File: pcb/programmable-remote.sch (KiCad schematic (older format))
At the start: 36 parts

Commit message: Initial schematic done.
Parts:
- removed R?: 20, symbol Device:R
- added Q1: Q_NPN_Darlington_BCE, Package_TO_SOT_SMD:TSOT-23_HandSoldering, symbol Device:Q_NPN_Darlington_BCE
- added R3: 10, Resistor_SMD:R_0603_1608Metric_Pad0.98x0.95mm_HandSolder, symbol Device:R
- added R4: 68k, Resistor_SMD:R_0603_1608Metric_Pad0.98x0.95mm_HandSolder, symbol Device:R
- added R7, R8: 4.7k, Resistor_SMD:R_0603_1608Metric_Pad0.98x0.95mm_HandSolder, symbol Device:R
- added SW8: SW_DIP_x02, programmable-remote:SW_2LP, symbol Switch:SW_DIP_x02
- 500m1: renamed from 500m; footprint (none) -> Fuse:Fuse_0603_1608Metric_Pad1.05x0.95mm_HandSolder
- BT1: renamed from BT?; footprint (none) -> programmable-remote:Battery
- C1, C10, C11, C2, C3, C4, C5, C6, C7, C8, C9: renamed from C?; footprint (none) -> Capacitor_SMD:C_0603_1608Metric_Pad1.08x0.95mm_HandSolder
- D1, D2: renamed from D?; footprint (none) -> Capacitor_SMD:C_0805_2012Metric_Pad1.18x1.45mm_HandSolder
- D3, D4: renamed from D?; footprint (none) -> Diode_SMD:D_1206_3216Metric_Pad1.42x1.75mm_HandSolder
- D5: renamed from D?; footprint (none) -> LED_THT:LED_D3.0mm_IRGrey
- J1: renamed from J?; footprint (none) -> Connector_PinHeader_2.54mm:PinHeader_1x04_P2.54mm_Vertical
- J2: renamed from J?; footprint (none) -> Connector_PinHeader_2.54mm:PinHeader_1x01_P2.54mm_Vertical
- R1, R2, R5, R6: renamed from R?; footprint (none) -> Resistor_SMD:R_0603_1608Metric_Pad0.98x0.95mm_HandSolder
- SW1, SW3, SW4, SW5, SW6, SW7: renamed from SW?; footprint (none) -> Button_Switch_Keyboard:SW_Cherry_MX_1.00u_PCB
- SW2: renamed from SW?; footprint (none) -> programmable-remote:SW_PTS526
- U2: renamed from U?; footprint (none) -> Package_SO:SOIC-8_3.9x4.9mm_P1.27mm
- Y1: renamed from Y?; footprint (none) -> programmable-remote:Crystal_ABLS-8.000MHZ-B4-T
- gave numbers to parts that had none: 2
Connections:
- net GND: now also Q1.3 (E), R7.2, R8.2; no longer D5.1 (K)
- net IR_OUT: now also R4.2
- net V3_3: now also D5.2 (A), SW8.1, SW8.2
- net BOOT1: now reaches U1.28 (PB2)
- net BOOT1: now also R7.1, SW8.3
- net BOOT0: now reaches U1.60 (BOOT0)
- net BOOT0: now also R8.1, SW8.4
- new net: D5.1 (K), R3.2
- new net: Q1.1 (B), R4.1
- new net: Q1.2 (C), R3.1
- no-connect marks 0 -> 33
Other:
- note added: "Assume saturation for the following:\nI_ledmax = 100 mA\nR_collector = (V3_3 - V_led - V_transistor)/l_ledmax\nR_collector = (3.3 - 1.42 - 1)/0.1 ohm = 8.8 ohm\nI_base = I_ledmax/Hfe*ODF = .1/50000*10 A = 20 uA\nR_base = (V3_3 - V_be) / I_base\n= (3.3 - 2) / 0.00002 ohm = 65 kohm\n"
- note added: "Switches"
- note removed: "Buttons"
- moved on the sheet: C8, D1, D2, D5, J2, R1, R2, R5, SW1, SW2, SW3, SW4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

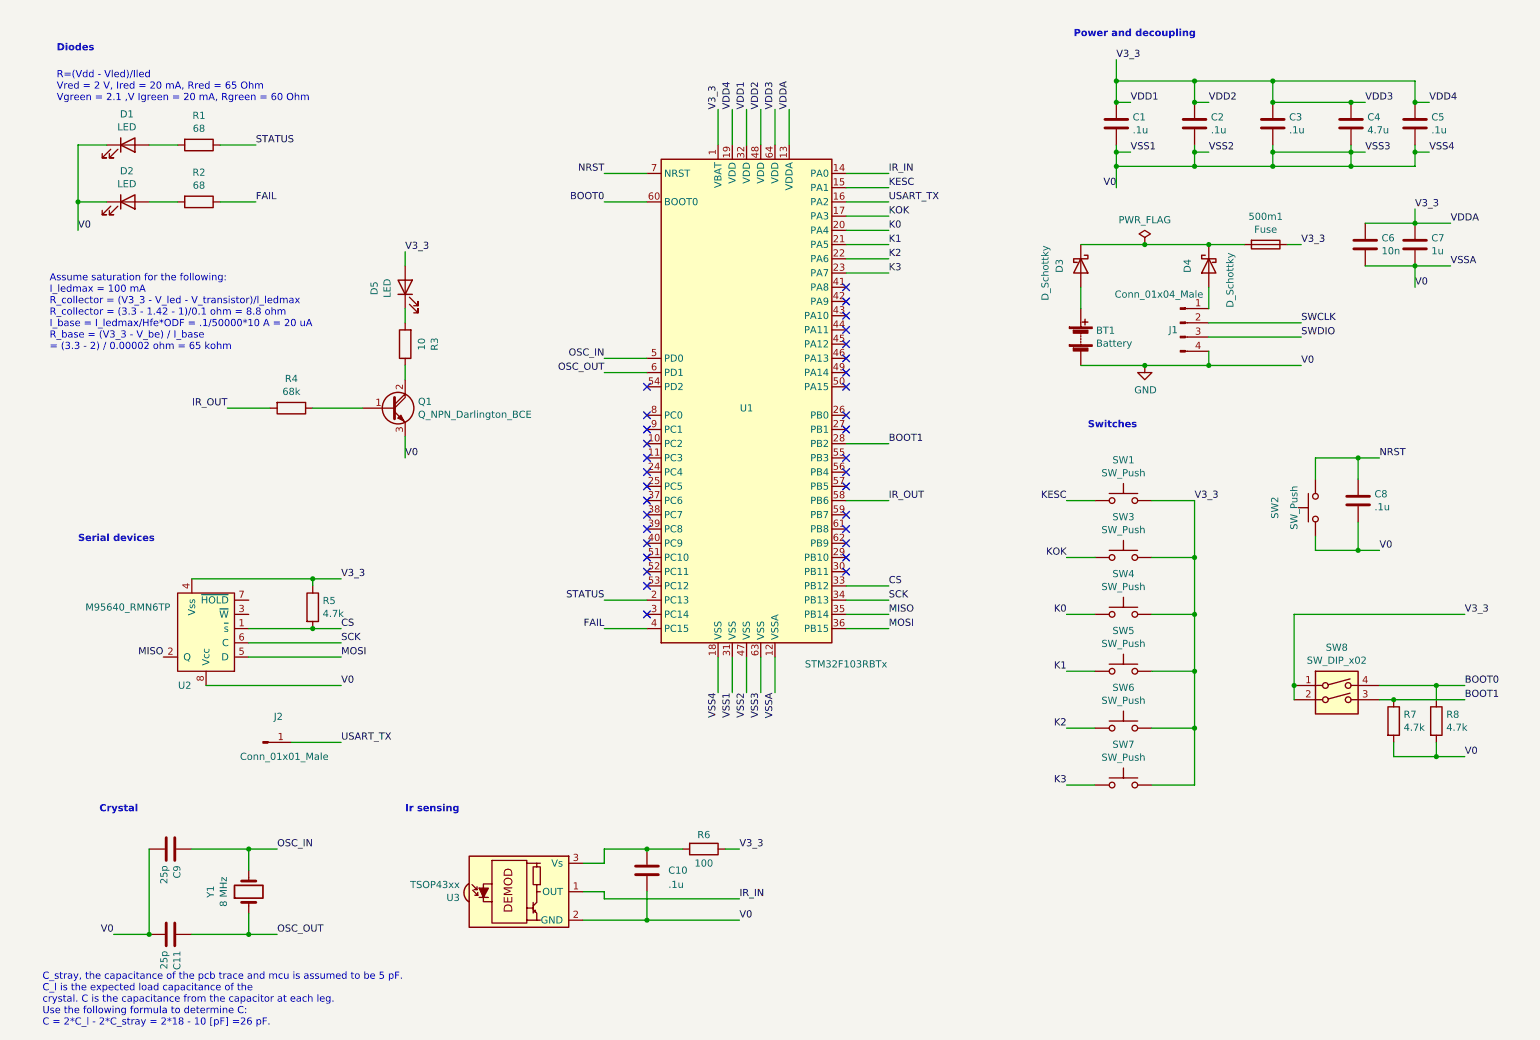
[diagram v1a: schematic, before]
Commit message: Fix drc errors.
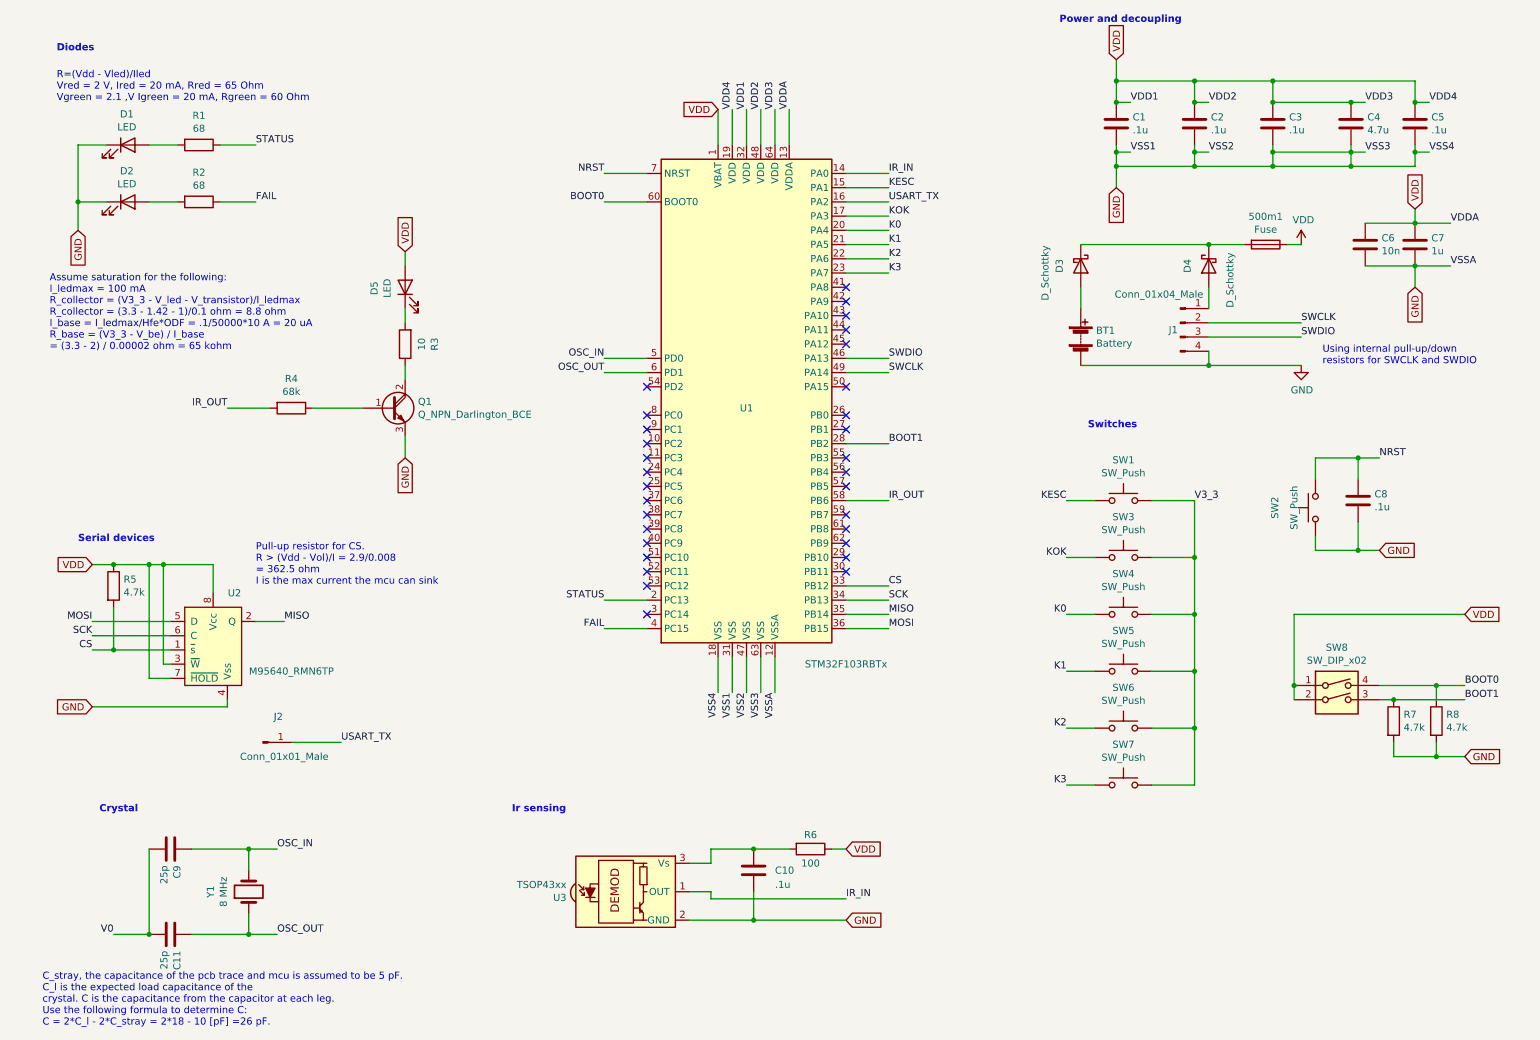
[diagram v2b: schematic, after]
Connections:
- net GND: now also U2.4 (Vss); no longer C11.2, C9.2, U2.8 (Vcc)
- net SWCLK: now also U1.49 (PA14)
- net SWDIO: now also U1.46 (PA13)
- net V3_3: no longer 500m1.1, C1.1, C2.1, C3.1, C4.1, C5.1, C6.1, C7.1, D5.2 (A), R5.1, R6.1, SW8.1, SW8.2, U1.1 (VBAT), U1.13 (VDDA), U1.19 (VDD), U1.32 (VDD), U1.48 (VDD), U1.64 (VDD), U2.4 (Vss)
- net VDD: now reaches U2.3 (~W)
- net VDD: now also 500m1.1, C1.1, C2.1, C3.1, C4.1, C5.1, C6.1, C7.1, D5.2 (A), R5.1, R6.1, SW8.1, SW8.2, U1.1 (VBAT), U1.13 (VDDA), U1.19 (VDD), U1.32 (VDD), U1.48 (VDD), U1.64 (VDD), U2.7 (~HOLD), U2.8 (Vcc)
- new net V0: C11.2, C9.2
- no-connect marks 33 -> 31
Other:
- note added: "Pull-up resistor for CS.\nR > (Vdd - Vol)/I = 2.9/0.008\n= 362.5 ohm\nI is the max current the mcu can sink"
- note added: "Using internal pull-up/down\nresistors for SWCLK and SWDIO\n"
- moved on the sheet: C10, R5, R6, U2, U3

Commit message: Started layout.
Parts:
- removed U3: TSOP43xx, OptoDevice:Vishay_MOLD-3Pin, symbol Interface_Optical:TSOP43xx
- added U3: TSOP953xx, programmable-remote:TSOP953xx, symbol programmable-remote:TSOP953xx
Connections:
- net V0 is gone; now on net GND: C11.2, C9.2
- net GND: now also U3.1 (GND)
- net IR_IN: now also U3.3 (OUT)
- net at C10.1, R6.2: now also U3.2 (Vs)
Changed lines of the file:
@@
-	1    0    0    -1
-$EndComp
-$Comp
-L Interface_Optical:TSOP43xx U3
-U 1 1 60BD0275
-P 4900 6750
-F 0 "U3" H 4434 6708 50  0000 R CNN
-F 1 "TSOP43xx" H 4434 6799 50  0000 R CNN
-F 2 "OptoDevice:Vishay_MOLD-3Pin" H 4850 6375 50  0001 C CNN
-F 3 "http://www.vishay.com/docs/82460/tsop45.pdf" H 5550 7050 50  0001 C CNN
-	1    4900 6750
 	1    0    0    -1
 $EndComp
@@
 	2850 5700 2500 5700
 Wire Wire Line
-	5300 6950 5750 6950
-Wire Wire Line
-	5750 6750 5750 6950
-Connection ~ 5750 6950
-Wire Wire Line
-	5750 6950 6400 6950
-Wire Wire Line
-	5300 6550 5450 6550
-Wire Wire Line
-	5450 6550 5450 6450
+	5750 6750 5750 6900
+Connection ~ 5750 6900
+Wire Wire Line
+	5750 6900 6400 6900
+Wire Wire Line
+	5300 6600 5450 6600
+Wire Wire Line
+	5450 6600 5450 6450
 Wire Wire Line
 	5450 6450 5750 6450
@@
 Wire Wire Line
 	6400 6800 5450 6800
-Wire Wire Line
-	5450 6800 5450 6750
-Wire Wire Line
-	5450 6750 5300 6750
 Text Label 6700 2000 0    50   ~ 0
 KOK
@@
 Wire Wire Line
 	2400 6450 2200 6450
-Text Label 1250 7050 2    50   ~ 0
-V0
 Wire Wire Line
 	1800 7050 2200 7050
@@
 	9400 1200 9950 1200
 Wire Wire Line
-	8300 1200 8300 1050
-Wire Wire Line
 	8850 1650 8850 1550
 Wire Wire Line
@@
 Wire Wire Line
 	10400 1200 10400 1050
-Wire Wire Line
-	10400 1050 9400 1050
-Wire Wire Line
-	8300 1050 8300 900
-Connection ~ 8300 1050
-Connection ~ 8850 1050
-Wire Wire Line
-	8850 1050 8300 1050
-Connection ~ 9400 1050
-Wire Wire Line
-	9400 1050 8850 1050
 Wire Wire Line
 	8300 1500 8300 1550
@@
 Text Notes 1150 6200 0    50   ~ 10
 Crystal
-Text Notes 4050 6200 0    50   ~ 10
+Text Notes 4250 6200 0    50   ~ 10
 Ir sensing
 Text Notes 750  7700 0    50   ~ 0
@@
 Text GLabel 10750 4800 2    50   Input ~ 0
 VDD
-Text GLabel 6400 6950 2    50   Input ~ 0
+Text GLabel 6400 6900 2    50   Input ~ 0
 GND
 Text GLabel 10750 5800 2    50   Input ~ 0
@@
 Text GLabel 5500 1250 0    50   Input ~ 0
 VDD
+Wire Wire Line
+	5450 6800 5450 6750
+Wire Wire Line
+	5450 6750 5300 6750
+$Comp
+L programmable-remote:TSOP953xx U3
+U 1 1 616AA23F
+P 5050 6850
+F 0 "U3" H 5103 7325 50  0000 C CNN
+F 1 "TSOP953xx" H 5103 7234 50  0000 C CNN
+F 2 "programmable-remote:TSOP953xx" H 5110 6850 50  0001 C CNN
+F 3 "" H 5110 6850 50  0001 C CNN
+	1    5050 6850
+	1    0    0    -1
+$EndComp
+Wire Wire Line
+	5300 6900 5750 6900
+Text GLabel 1250 7050 0    50   Input ~ 0
+GND
+Wire Wire Line
+	8300 900  8300 1200
+Text GLabel 8850 1050 1    50   Input ~ 0
+VDD
+Text GLabel 9400 1050 1    50   Input ~ 0
+VDD
+Text GLabel 10400 1050 1    50   Input ~ 0
+VDD
 $EndSCHEMATC

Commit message: signals routed
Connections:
- net V3_3 is gone; now on net VDD: SW1.2, SW3.2, SW4.2, SW5.2, SW6.2, SW7.2
- net IR_Pwr2: now reaches D5.1 (K), R3.2
- net BAT+: now reaches BT1.1 (+), D3.2 (A)
- net SWD_VDD: now reaches D4.2 (A), J1.1 (Pin_1)
- net IR_Pwr1: now reaches Q1.2 (C), R3.1
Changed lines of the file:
@@
 Wire Wire Line
 	7950 6000 8150 6000
-Text Label 8850 4000 0    50   ~ 0
-V3_3
 $Comp
 L Device:C C8
@@
 Text GLabel 10400 1050 1    50   Input ~ 0
 VDD
+Text Label 3300 3100 0    50   ~ 0
+IR_Pwr1
+Text Label 3300 2700 0    50   ~ 0
+IR_Pwr2
+Text Label 8050 2600 0    50   ~ 0
+BAT+
+Text Label 8950 2550 0    50   ~ 0
+SWD_VDD
+Text GLabel 8850 4000 2    50   Input ~ 0
+VDD
 $EndSCHEMATC

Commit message: Pcb 1.0
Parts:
- added TP1, TP2, TP3, TP4, TP5, TP6, TP7, TP8: TestPoint, programmable-remote:TestPoint_harwin_S2761-46R, symbol Connector:TestPoint
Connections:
- net CS: now also TP6.1
- net IR_IN: now also TP7.1
- net IR_Pwr2: now also TP1.1
- net MISO: now also TP4.1
- net MOSI: now also TP3.1
- net SCK: now also TP5.1
- net VDD: now also TP8.1
- net at Q1.1 (B), R4.1: now also TP2.1
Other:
- moved on the sheet: J2, R5, U2
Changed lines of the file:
@@
 L Connector:Conn_01x01_Male J2
 U 1 1 60BCCB41
-P 2300 5700
-F 0 "J2" H 2408 5881 50  0000 C CNN
-F 1 "Conn_01x01_Male" H 2450 5600 50  0000 C CNN
-F 2 "Connector_PinHeader_2.54mm:PinHeader_1x01_P2.54mm_Vertical" H 2300 5700 50  0001 C CNN
-F 3 "~" H 2300 5700 50  0001 C CNN
-	1    2300 5700
+P 2430 5680
+F 0 "J2" H 2538 5861 50  0000 C CNN
+F 1 "Conn_01x01_Male" H 2580 5580 50  0000 C CNN
+F 2 "Connector_PinHeader_2.54mm:PinHeader_1x01_P2.54mm_Vertical" H 2430 5680 50  0001 C CNN
+F 3 "~" H 2430 5680 50  0001 C CNN
+	1    2430 5680
 	1    0    0    -1
 $EndComp
@@
 Text Label 2250 1900 0    50   ~ 0
 FAIL
-Text Label 2850 5700 0    50   ~ 0
+Text Label 2980 5680 0    50   ~ 0
 USART_TX
 $Comp
@@
 U 1 1 60BE8135
 P 5750 6600
-F 0 "C10" H 5900 6600 50  0000 L CNN
-F 1 ".1u" H 5900 6500 50  0000 L CNN
+F 0 "C10" H 5570 6690 50  0000 L CNN
+F 1 ".1u" H 5610 6500 50  0000 L CNN
 F 2 "Capacitor_SMD:C_0603_1608Metric_Pad1.08x0.95mm_HandSolder" H 5788 6450 50  0001 C CNN
 F 3 "~" H 5750 6600 50  0001 C CNN
@@
 L programmable-remote:M95640_RMN6TP U2
 U 1 1 610CB268
-P 1950 5100
-F 0 "U2" H 2100 5550 50  0000 C CNN
-F 1 "M95640_RMN6TP" H 2500 5000 50  0000 C CNN
-F 2 "Package_SO:SOIC-8_3.9x4.9mm_P1.27mm" H 1950 5100 50  0001 C CNN
-F 3 "" H 1950 5100 50  0001 C CNN
-	1    1950 5100
+P 2080 5080
+F 0 "U2" H 2230 5530 50  0000 C CNN
+F 1 "M95640_RMN6TP" H 2630 4980 50  0000 C CNN
+F 2 "Package_SO:SOIC-8_3.9x4.9mm_P1.27mm" H 2080 5080 50  0001 C CNN
+F 3 "" H 2080 5080 50  0001 C CNN
+	1    2080 5080
 	1    0    0    -1
 $EndComp
@@
 F 3 "~" V 8050 2910 50  0001 C CNN
 	1    8050 2850
-	1    0    0    -1
-$EndComp
-$Comp
-L Device:R R5
-U 1 1 610D8C9C
-P 1250 4600
-F 0 "R5" H 1320 4646 50  0000 L CNN
-F 1 "4.7k" H 1320 4555 50  0000 L CNN
-F 2 "Resistor_SMD:R_0603_1608Metric_Pad0.98x0.95mm_HandSolder" V 1180 4600 50  0001 C CNN
-F 3 "~" H 1250 4600 50  0001 C CNN
-	1    1250 4600
 	1    0    0    -1
 $EndComp
@@
 	0    -1   1    0
 $EndComp
-Text Label 1100 5050 2    50   ~ 0
-CS
-Text Label 1100 4950 2    50   ~ 0
+Text Label 1230 4930 2    50   ~ 0
 SCK
-Text Label 1100 4850 2    50   ~ 0
+Text Label 1230 4830 2    50   ~ 0
 MOSI
-Text Label 2450 4850 0    50   ~ 0
+Text Label 2580 4830 0    50   ~ 0
 MISO
 Wire Wire Line
@@
 IR_IN
 Wire Wire Line
-	2850 5700 2500 5700
+	2980 5680 2630 5680
 Wire Wire Line
 	5750 6750 5750 6900
@@
 Wire Wire Line
 	6300 6450 6400 6450
-Wire Wire Line
-	6400 6800 5450 6800
 Text Label 6700 2000 0    50   ~ 0
 KOK
@@
 Text Label 2050 3350 2    50   ~ 0
 IR_OUT
-Text Notes 1000 4300 0    50   ~ 10
+Text Notes 1130 4280 0    50   ~ 10
 Serial devices
 $Comp
@@
 $EndComp
 Wire Wire Line
-	3300 2650 3300 2750
+	3300 2650 3300 2700
 Wire Wire Line
 	3300 3050 3300 3150
@@
 	2050 3350 2350 3350
 Wire Wire Line
-	2650 3350 3000 3350
-Text Notes 800  2950 0    50   ~ 0
+	2650 3350 2750 3350
+Text Notes 650  3100 0    50   ~ 0
 Assume saturation for the following:\nI_ledmax = 100 mA\nR_collector = (V3_3 - V_led - V_transistor)/l_ledmax\nR_collector = (3.3 - 1.42 - 1)/0.1 ohm = 8.8 ohm\nI_base = I_ledmax/Hfe*ODF = .1/50000*10 A = 20 uA\nR_base = (V3_3 - V_be) / I_base\n= (3.3 - 2) / 0.00002 ohm = 65 kohm\n
 $Comp
@@
 	9500 2200 9600 2200
 Wire Wire Line
-	1100 4450 1250 4450
-Wire Wire Line
-	1250 4450 1500 4450
-Wire Wire Line
-	1950 4450 1950 4650
-Connection ~ 1250 4450
-Wire Wire Line
-	1100 4850 1650 4850
-Wire Wire Line
-	1100 4950 1650 4950
-Wire Wire Line
-	1100 5050 1250 5050
-Wire Wire Line
-	1250 4750 1250 5050
-Connection ~ 1250 5050
-Wire Wire Line
-	1250 5050 1650 5050
-Wire Wire Line
-	1100 5450 2050 5450
-Wire Wire Line
-	2050 5450 2050 5400
-Wire Wire Line
-	2250 4850 2450 4850
-Wire Wire Line
-	1650 5150 1600 5150
-Wire Wire Line
-	1600 5150 1600 4450
-Connection ~ 1600 4450
-Wire Wire Line
-	1600 4450 1950 4450
-Wire Wire Line
-	1650 5250 1500 5250
-Wire Wire Line
-	1500 5250 1500 4450
-Connection ~ 1500 4450
-Wire Wire Line
-	1500 4450 1600 4450
-Text Notes 2250 4600 0    50   ~ 0
+	2080 4430 2080 4630
+Wire Wire Line
+	1230 5430 2180 5430
+Wire Wire Line
+	2180 5430 2180 5380
+Wire Wire Line
+	2380 4830 2430 4830
+Wire Wire Line
+	1780 5130 1730 5130
+Wire Wire Line
+	1730 5130 1730 4430
+Connection ~ 1730 4430
+Wire Wire Line
+	1730 4430 2080 4430
+Wire Wire Line
+	1780 5230 1630 5230
+Wire Wire Line
+	1630 5230 1630 4430
+Connection ~ 1630 4430
+Wire Wire Line
+	1630 4430 1730 4430
+Text Notes 2380 4580 0    50   ~ 0
 Pull-up resistor for CS.\nR > (Vdd - Vol)/I = 2.9/0.008\n= 362.5 ohm\nI is the max current the mcu can sink
 Text Label 6700 3000 0    50   ~ 0
@@
 Text GLabel 6400 6450 2    50   Input ~ 0
 VDD
-Text GLabel 1100 4450 0    50   Input ~ 0
+Text GLabel 1230 4430 0    50   Input ~ 0
 VDD
-Text GLabel 1100 5450 0    50   Input ~ 0
+Text GLabel 1230 5430 0    50   Input ~ 0
 GND
 Text GLabel 3300 2250 1    50   Input ~ 0
@@
 Text GLabel 8850 4000 2    50   Input ~ 0
 VDD
+$Comp
+L Connector:TestPoint TP4
+U 1 1 611DB70E
+P 2430 4830
+F 0 "TP4" H 2488 4948 50  0000 L CNN
+F 1 "TestPoint" H 2480 5030 50  0000 L CNN
+F 2 "programmable-remote:TestPoint_harwin_S2761-46R" H 2630 4830 50  0001 C CNN
+F 3 "~" H 2630 4830 50  0001 C CNN
+	1    2430 4830
+	1    0    0    -1
+$EndComp
+Connection ~ 2430 4830
+Wire Wire Line
+	2430 4830 2580 4830
+Text Label 1230 5030 2    50   ~ 0
+CS
+Wire Wire Line
+	1380 5030 1780 5030
+Connection ~ 1380 5030
+Wire Wire Line
+	1380 4730 1380 5030
+Connection ~ 1380 4430
+Wire Wire Line
+	1380 4430 1630 4430
+Wire Wire Line
+	1230 4430 1380 4430
+$Comp
+L Device:R R5
+U 1 1 610D8C9C
+P 1380 4580
+F 0 "R5" H 1450 4626 50  0000 L CNN
+F 1 "4.7k" H 1450 4535 50  0000 L CNN
+F 2 "Resistor_SMD:R_0603_1608Metric_Pad0.98x0.95mm_HandSolder" V 1310 4580 50  0001 C CNN
+F 3 "~" H 1380 4580 50  0001 C CNN
+	1    1380 4580
+	1    0    0    -1
+$EndComp
+$Comp
+L Connector:TestPoint TP3
+U 1 1 6120B96A
+P 1100 4830
+F 0 "TP3" V 1220 5150 50  0000 C CNN
+F 1 "TestPoint" V 1150 5180 50  0000 C CNN
+F 2 "programmable-remote:TestPoint_harwin_S2761-46R" H 1300 4830 50  0001 C CNN
+F 3 "~" H 1300 4830 50  0001 C CNN
+	1    1100 4830
+	0    -1   -1   0
+$EndComp
+$Comp
+L Connector:TestPoint TP5
+U 1 1 6120C2C0
+P 1100 4930
+F 0 "TP5" V 1140 5250 50  0000 C CNN
+F 1 "TestPoint" V 1070 5270 50  0000 C CNN
+F 2 "programmable-remote:TestPoint_harwin_S2761-46R" H 1300 4930 50  0001 C CNN
+F 3 "~" H 1300 4930 50  0001 C CNN
+	1    1100 4930
+	0    -1   -1   0
+$EndComp
+$Comp
+L Connector:TestPoint TP6
+U 1 1 6120CA73
+P 1100 5030
+F 0 "TP6" V 1030 5260 50  0000 C CNN
+F 1 "TestPoint" V 950 5260 50  0000 C CNN
+F 2 "programmable-remote:TestPoint_harwin_S2761-46R" H 1300 5030 50  0001 C CNN
+F 3 "~" H 1300 5030 50  0001 C CNN
+	1    1100 5030
+	0    -1   -1   0
+$EndComp
+Wire Wire Line
+	1100 4830 1780 4830
+Wire Wire Line
+	1100 4930 1780 4930
+Wire Wire Line
+	1100 5030 1380 5030
+$Comp
+L Connector:TestPoint TP2
+U 1 1 6123CA6F
+P 2750 3350
+F 0 "TP2" H 2808 3468 50  0000 L CNN
+F 1 "TestPoint" H 2808 3377 50  0000 L CNN
+F 2 "programmable-remote:TestPoint_harwin_S2761-46R" H 2950 3350 50  0001 C CNN
+F 3 "~" H 2950 3350 50  0001 C CNN
+	1    2750 3350
+	1    0    0    -1
+$EndComp
+Connection ~ 2750 3350
+Wire Wire Line
+	2750 3350 3000 3350
+$Comp
+L Connector:TestPoint TP1
+U 1 1 6123D980
+P 3300 2700
+F 0 "TP1" V 3254 2888 50  0000 L CNN
+F 1 "TestPoint" V 3345 2888 50  0000 L CNN
+F 2 "programmable-remote:TestPoint_harwin_S2761-46R" H 3500 2700 50  0001 C CNN
+F 3 "~" H 3500 2700 50  0001 C CNN
+	1    3300 2700
+	0    -1   -1   0
+$EndComp
+$Comp
+L Connector:TestPoint TP7
+U 1 1 6124931E
+P 5990 6800
+F 0 "TP7" H 6040 6940 50  0000 L CNN
+F 1 "TestPoint" H 6020 6860 50  0000 L CNN
+F 2 "programmable-remote:TestPoint_harwin_S2761-46R" H 6190 6800 50  0001 C CNN
+F 3 "~" H 6190 6800 50  0001 C CNN
+	1    5990 6800
+	1    0    0    -1
+$EndComp
+Connection ~ 5990 6800
+Wire Wire Line
+	5990 6800 5450 6800
+Wire Wire Line
+	5990 6800 6400 6800
+$Comp
+L Connector:TestPoint TP8
+U 1 1 61183496
+P 9600 2200
+F 0 "TP8" V 9500 2300 50  0000 L CNN
+F 1 "TestPoint" V 9700 2200 50  0000 L CNN
+F 2 "programmable-remote:TestPoint_harwin_S2761-46R" H 9800 2200 50  0001 C CNN
+F 3 "~" H 9800 2200 50  0001 C CNN
+	1    9600 2200
+	0    1    1    0
+$EndComp
+Connection ~ 9600 2200
+Connection ~ 3300 2700
+Wire Wire Line
+	3300 2700 3300 2750
 $EndSCHEMATC
